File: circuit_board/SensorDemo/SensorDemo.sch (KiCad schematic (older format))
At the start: 58 parts, among them K1 PB, P1 CONN3X2, P2 CONN3X2, U1 TLV1117-33CDCYR, U2 dsPIC33EP32GP502, U3 LTC1658, U4 INA126, U5 REF1925, U6 REF1925, X1 8MHz

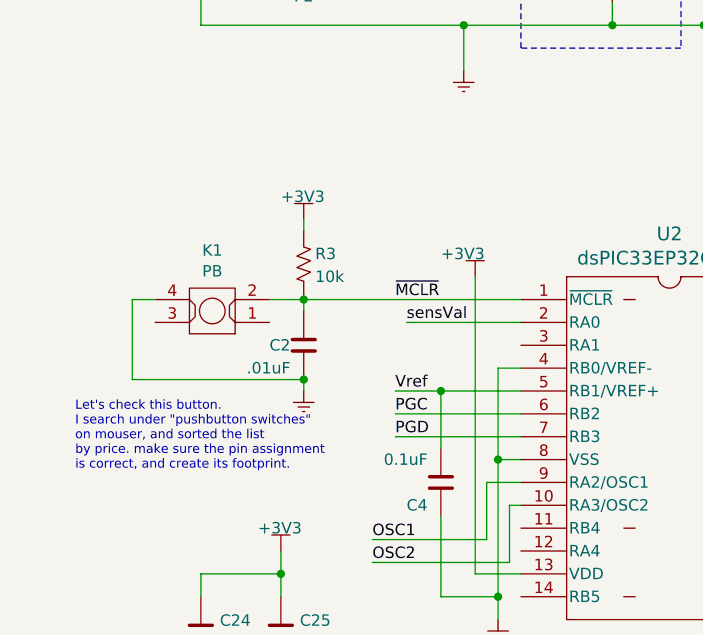
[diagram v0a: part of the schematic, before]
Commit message: reset key modified
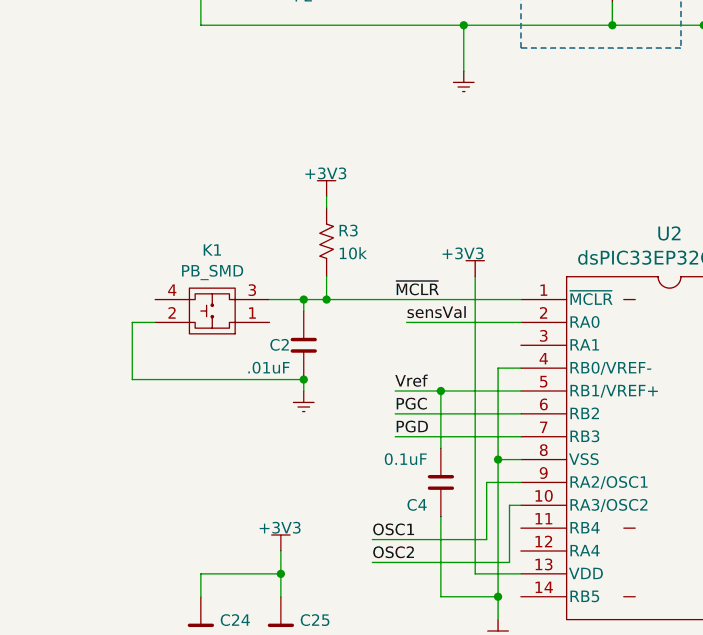
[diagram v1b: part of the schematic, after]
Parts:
- removed K1: PB, SensorDemo_pcb:SOT-23-4, symbol SensorDemo_discrete:PB
- added K1: PB_SMD, SensorDemo_pcb:Key_SMD, symbol SensorDemo_discrete:PB_SMD
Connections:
- net ~MCLR: now also K1.3
- net at C2.2: now also K1.2
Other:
- note removed: "Let's check this button. \nI search under "pushbutton switches"\non mouser, and sorted the list\nby price. make sure the pin assignment\nis correct, and create its footprint."
- moved on the sheet: R3
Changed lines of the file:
@@
 L SensorDemo_passive:R R3
 U 1 1 602D3910
-P 1800 2900
-F 0 "R3" V 1750 2950 50  0000 L CNN
-F 1 "10k" V 1850 2950 50  0000 L CNN
-F 2 "SensorDemo_pcb:R0805" H 1750 2830 30  0001 C CNN
-F 3 "" V 1800 2900 30  0000 C CNN
-	1    1800 2900
+P 1900 2800
+F 0 "R3" V 1850 2850 50  0000 L CNN
+F 1 "10k" V 1950 2850 50  0000 L CNN
+F 2 "SensorDemo_pcb:R0805" H 1850 2730 30  0001 C CNN
+F 3 "" V 1900 2800 30  0000 C CNN
+	1    1900 2800
 	0    1    1    0
 $EndComp
@@
 	1800 3400 1800 3450
 Wire Wire Line
-	1800 2700 1800 2750
+	1900 2600 1900 2650
 Wire Wire Line
 	10150 1150 9950 1150
@@
 	1    0    0    -1
 $EndComp
-$Comp
-L SensorDemo_discrete:PB K1
-U 1 1 60393582
-P 1400 3100
-F 0 "K1" H 1400 2835 50  0000 C CNN
-F 1 "PB" H 1400 2926 50  0000 C CNN
-F 2 "SensorDemo_pcb:SOT-23-4" H 1400 2950 60  0001 C CNN
-F 3 "https://www.mouser.com/ProductDetail/E-Switch/LL3301NF065QG/?qs=QtyuwXswaQiWhwgY68YTTw%3D%3D" H 1400 2950 60  0001 C CNN
-	1    1400 3100
-	-1   0    0    1
-$EndComp
 Wire Wire Line
 	1800 3050 1800 3100
 Wire Wire Line
 	1800 3050 1650 3050
-Wire Wire Line
-	1150 3050 1050 3050
-Wire Wire Line
-	1050 3050 1050 3400
 Wire Wire Line
 	1050 3400 1800 3400
@@
 L SensorDemo_power_supply:+3V3 #PS0104
 U 1 1 603D7984
-P 1800 2700
-F 0 "#PS0104" H 1800 2650 50  0001 C CNN
-F 1 "+3V3" H 1700 2800 50  0000 L CNN
-F 2 "" H 1805 2395 50  0001 C CNN
-F 3 "" H 1805 2395 50  0001 C CNN
-	1    1800 2700
+P 1900 2600
+F 0 "#PS0104" H 1900 2550 50  0001 C CNN
+F 1 "+3V3" H 1800 2700 50  0000 L CNN
+F 2 "" H 1905 2295 50  0001 C CNN
+F 3 "" H 1905 2295 50  0001 C CNN
+	1    1900 2600
 	1    0    0    -1
 $EndComp
@@
 	2650 4350 2650 3750
 Wire Wire Line
-	1800 3050 2750 3050
+	1800 3050 1900 3050
 $Comp
 L SensorDemo_passive:C C19
@@
 	1    0    0    -1
 $EndComp
-Text Notes 800  3800 0    40   ~ 0
-Let's check this button. \nI search under "pushbutton switches"\non mouser, and sorted the list\nby price. make sure the pin assignment\nis correct, and create its footprint.
 Text Label 2500 6700 0    50   ~ 0
 PGC
@@
 NoConn ~ 3450 6700
 $Comp
-L SensorDemo_power_supply:GND #PS?
+L SensorDemo_power_supply:GND #PS0126
 U 1 1 6063F2B2
 P 2400 6800
-F 0 "#PS?" H 2400 6675 50  0001 C CNN
+F 0 "#PS0126" H 2400 6675 50  0001 C CNN
 F 1 "GND" H 2400 6725 50  0001 C CNN
 F 2 "" H 2400 6800 50  0001 C CNN
@@
 	2400 6600 2750 6600
 $Comp
-L SensorDemo_power_supply:+3V3 #PS?
+L SensorDemo_power_supply:+3V3 #PS0127
 U 1 1 6064F95D
 P 3700 6350
-F 0 "#PS?" H 3700 6300 50  0001 C CNN
+F 0 "#PS0127" H 3700 6300 50  0001 C CNN
 F 1 "+3V3" H 3600 6450 50  0000 L CNN
 F 2 "" H 3705 6045 50  0001 C CNN
@@
 Wire Wire Line
 	3700 6500 3700 6350
+$Comp
+L SensorDemo_discrete:PB_SMD K1
+U 1 1 60479CF2
+P 1400 3100
+F 0 "K1" H 1400 2835 50  0000 C CNN
+F 1 "PB_SMD" H 1400 2926 50  0000 C CNN
+F 2 "SensorDemo_pcb:Key_SMD" H 1400 2950 60  0001 C CNN
+F 3 "https://www.mouser.com/ProductDetail/E-Switch/LL3301NF065QG/?qs=QtyuwXswaQiWhwgY68YTTw%3D%3D" H 1400 2950 60  0001 C CNN
+	1    1400 3100
+	-1   0    0    1
+$EndComp
+Wire Wire Line
+	1150 3150 1050 3150
+Wire Wire Line
+	1050 3150 1050 3400
+Wire Wire Line
+	1900 2950 1900 3050
+Connection ~ 1900 3050
+Wire Wire Line
+	1900 3050 2750 3050
 $EndSCHEMATC

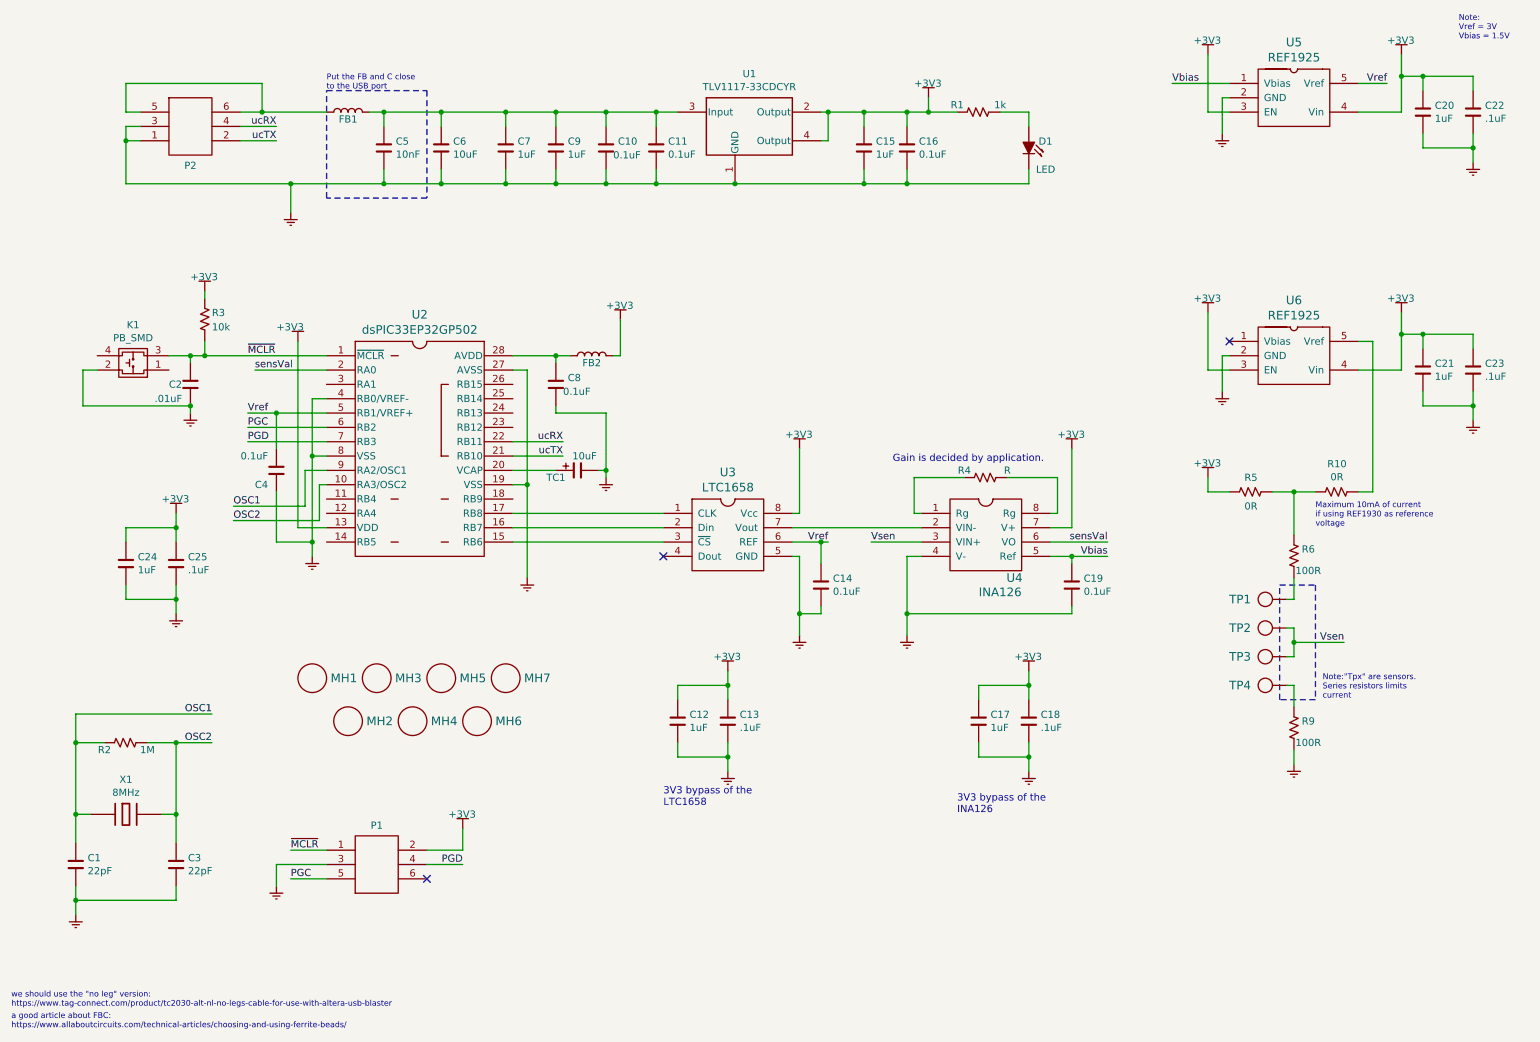
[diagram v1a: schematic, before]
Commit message: updated SensoDemo and ProgramBoard
INA126 is replaced by INA333.
TC2050-IDC-NL cable will be used for powering and programming.
both boards should be done.
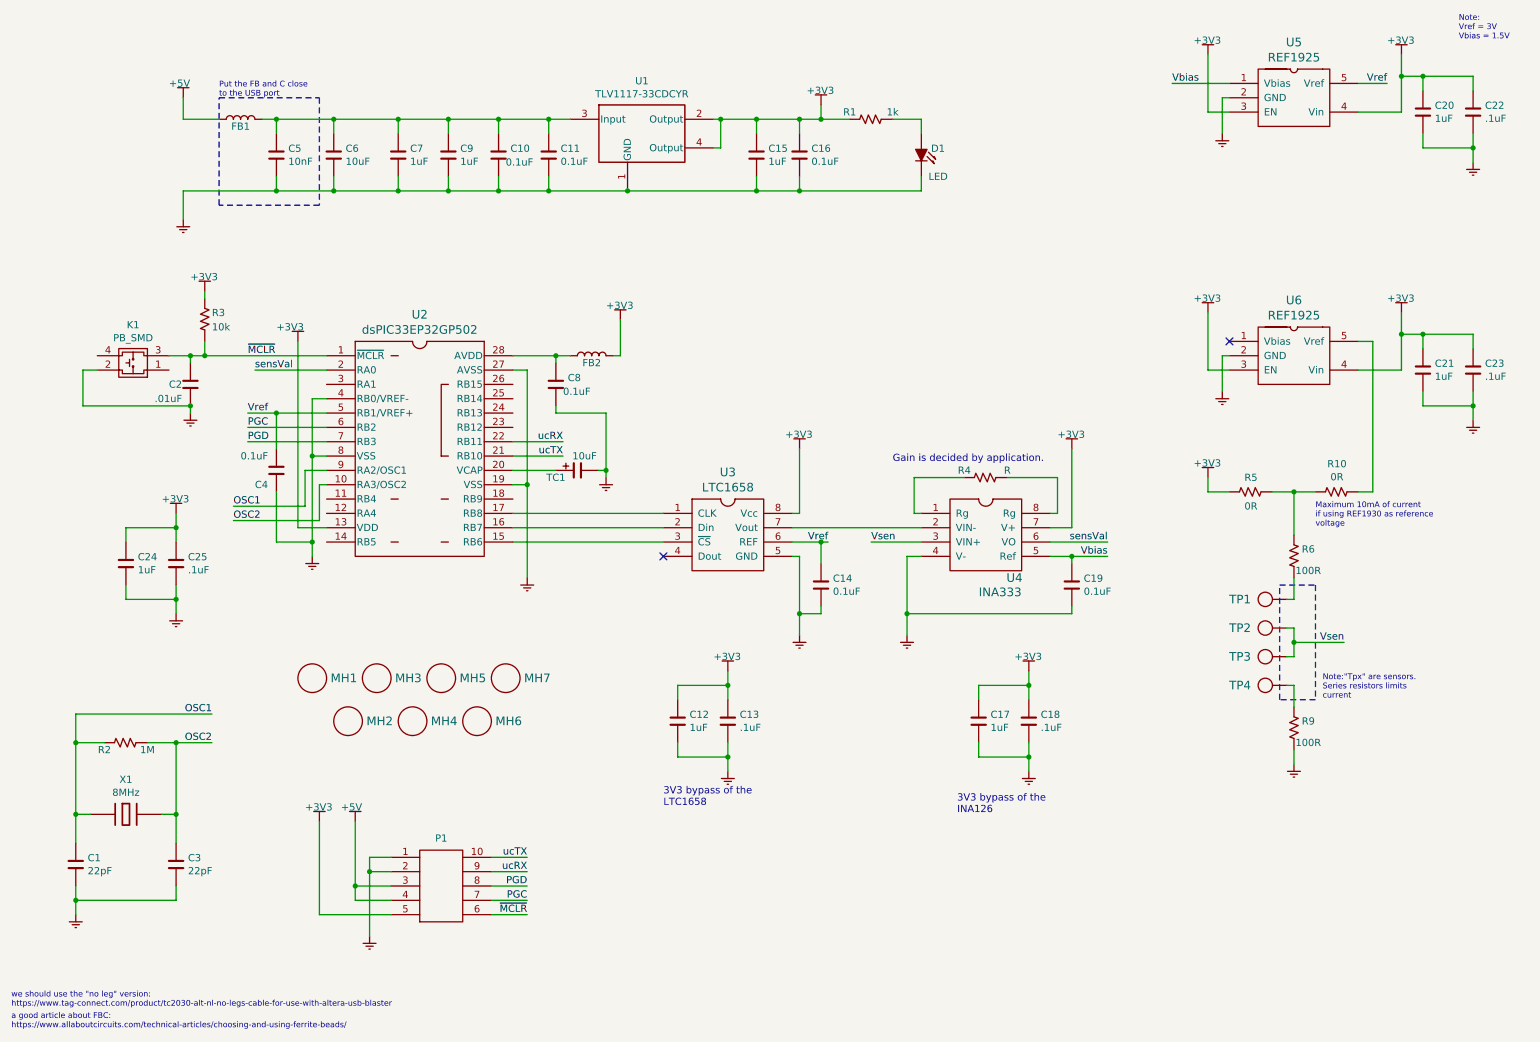
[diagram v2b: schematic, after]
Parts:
- removed P1, P2: CONN3X2, SensorDemo_pcb:TC2030, symbol SensorDemo_connector:CONN3X2
- added P1: TC2050_IDC_NL, SensorDemo_pcb:TC2050, symbol SensorDemo_connector:TC2050_IDC_NL
- U4: value INA126 -> INA333; footprint SensorDemo_pcb:SOIC-8 -> SensorDemo_pcb:MSOP-8
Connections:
- net PGC: now also P1.7
- net PGD: now also P1.8
- net ucRX: now also P1.9
- net ucTX: now also P1.10
- net ~MCLR: now also P1.6
- new net: P1.1, P1.2
- new net: P1.3, P1.4
- no-connect marks 3 -> 2
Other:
- moved on the sheet: C10, C11, C15, C16, C5, C6, C7, C9, D1, FB1, R1, U1
